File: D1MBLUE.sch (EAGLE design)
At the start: 7 parts, among them U1 HC_05

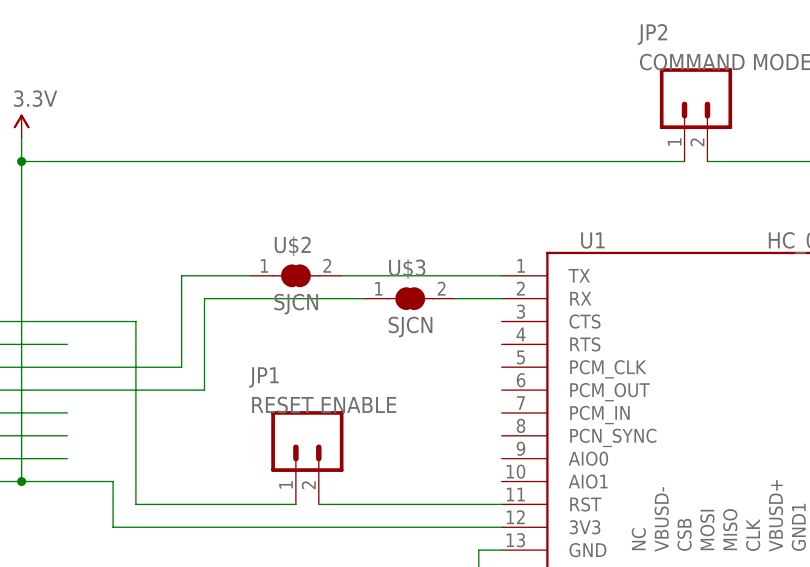
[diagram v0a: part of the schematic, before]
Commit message: Improved silkscreen and updated preview images
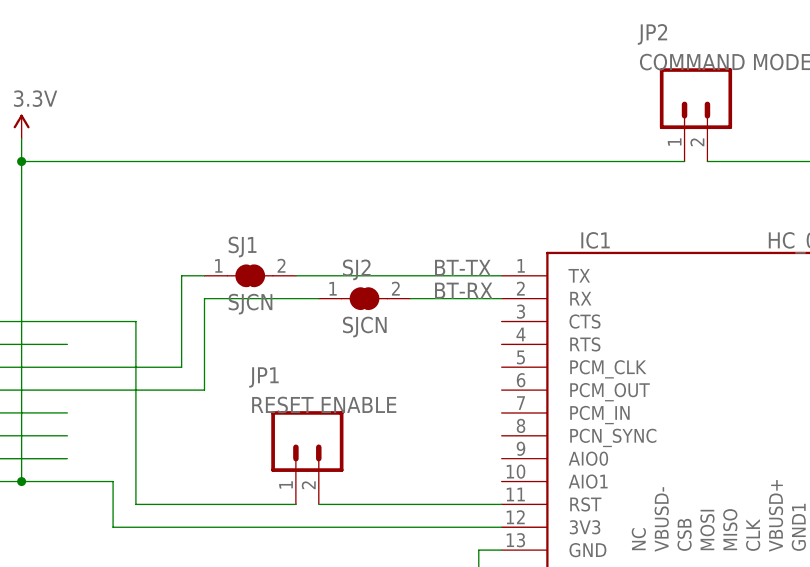
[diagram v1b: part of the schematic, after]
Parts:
- removed U$2, U$3: SJCN, freetronics-jon:SJCN
- added SJ1, SJ2: SJCN, freetronics-jon:SJCN
- renumbered U1 to IC1
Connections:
- removed net N$2: IC1.TX, U$2.2
- removed net N$4: IC1.RX, U$3.2
- new net BT-RX: IC1.RX, SJ2.2
- new net BT-TX: IC1.TX, SJ1.2
- net D0: now also SJ1.1; no longer U$2.1
- net D5: now also SJ2.1; no longer U$3.1
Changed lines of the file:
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@@
 <part name="P+1" library="freetronics-original" deviceset="3.3V" device=""/>
 <part name="GND1" library="freetronics-original" deviceset="GND" device=""/>
-<part name="U1" library="freetronics-jon" deviceset="HC_05" device=""/>
+<part name="IC1" library="freetronics-jon" deviceset="HC_05" device=""/>
 <part name="GND2" library="freetronics-original" deviceset="GND" device=""/>
 <part name="JP1" library="freetronics-jon" deviceset="M02" device="PTH" value="RESET ENABLE"/>
 <part name="JP2" library="freetronics-jon" deviceset="M02" device="PTH" value="COMMAND MODE"/>
-<part name="U$2" library="freetronics-jon" deviceset="SJC" device="N"/>
-<part name="U$3" library="freetronics-jon" deviceset="SJC" device="N"/>
+<part name="SJ1" library="freetronics-jon" deviceset="SJC" device="N"/>
+<part name="SJ2" library="freetronics-jon" deviceset="SJC" device="N"/>
 </parts>
 <sheets>
@@
 <instance part="P+1" gate="G$1" x="45.72" y="132.08"/>
 <instance part="GND1" gate="1" x="208.28" y="83.82"/>
-<instance part="U1" gate="G$1" x="121.92" y="101.6"/>
+<instance part="IC1" gate="G$1" x="121.92" y="101.6"/>
 <instance part="GND2" gate="1" x="149.86" y="71.12"/>
 <instance part="JP1" gate="G$1" x="76.2" y="99.06" smashed="yes" rot="R270">
@@
 <attribute name="NAME" x="114.3" y="143.002" size="1.778" layer="95"/>
 </instance>
-<instance part="U$2" gate="G$1" x="76.2" y="116.84"/>
-<instance part="U$3" gate="G$1" x="88.9" y="114.3"/>
+<instance part="SJ1" gate="G$1" x="71.12" y="116.84"/>
+<instance part="SJ2" gate="G$1" x="83.82" y="114.3"/>
 </instances>
 <busses>
@@
 </segment>
 <segment>
-<pinref part="U1" gate="G$1" pin="GND2"/>
+<pinref part="IC1" gate="G$1" pin="GND2"/>
 <pinref part="GND2" gate="1" pin="GND"/>
 <wire x1="147.32" y1="86.36" x2="149.86" y2="86.36" width="0.1524" layer="91"/>
 <wire x1="149.86" y1="86.36" x2="149.86" y2="76.2" width="0.1524" layer="91"/>
-<pinref part="U1" gate="G$1" pin="GND1"/>
+<pinref part="IC1" gate="G$1" pin="GND1"/>
 <wire x1="149.86" y1="76.2" x2="149.86" y2="73.66" width="0.1524" layer="91"/>
 <wire x1="132.08" y1="78.74" x2="132.08" y2="76.2" width="0.1524" layer="91"/>
 <wire x1="132.08" y1="76.2" x2="149.86" y2="76.2" width="0.1524" layer="91"/>
-<pinref part="U1" gate="G$1" pin="GND"/>
+<pinref part="IC1" gate="G$1" pin="GND"/>
 <wire x1="99.06" y1="86.36" x2="96.52" y2="86.36" width="0.1524" layer="91"/>
 <wire x1="96.52" y1="86.36" x2="96.52" y2="76.2" width="0.1524" layer="91"/>
@@
 <wire x1="31.75" y1="104.14" x2="66.04" y2="104.14" width="0.1524" layer="91"/>
 <label x="33.02" y="104.14" size="1.778" layer="95"/>
-<pinref part="U$3" gate="G$1" pin="1"/>
-<wire x1="83.82" y1="114.3" x2="66.04" y2="114.3" width="0.1524" layer="91"/>
+<pinref part="SJ2" gate="G$1" pin="1"/>
+<wire x1="78.74" y1="114.3" x2="66.04" y2="114.3" width="0.1524" layer="91"/>
 <wire x1="66.04" y1="114.3" x2="66.04" y2="104.14" width="0.1524" layer="91"/>
 </segment>
@@
 <label x="33.02" y="106.68" size="1.778" layer="95"/>
 <wire x1="63.5" y1="106.68" x2="63.5" y2="116.84" width="0.1524" layer="91"/>
-<pinref part="U$2" gate="G$1" pin="1"/>
-<wire x1="63.5" y1="116.84" x2="71.12" y2="116.84" width="0.1524" layer="91"/>
+<pinref part="SJ1" gate="G$1" pin="1"/>
+<wire x1="63.5" y1="116.84" x2="66.04" y2="116.84" width="0.1524" layer="91"/>
 </segment>
 </net>
@@
 <wire x1="45.72" y1="93.98" x2="45.72" y2="129.54" width="0.1524" layer="91"/>
 <junction x="45.72" y="93.98"/>
-<pinref part="U1" gate="G$1" pin="3V3"/>
+<pinref part="IC1" gate="G$1" pin="3V3"/>
 <wire x1="45.72" y1="129.54" x2="45.72" y2="132.08" width="0.1524" layer="91"/>
 <wire x1="99.06" y1="88.9" x2="55.88" y2="88.9" width="0.1524" layer="91"/>
@@
 <net name="N$1" class="0">
 <segment>
-<pinref part="U1" gate="G$1" pin="RST"/>
+<pinref part="IC1" gate="G$1" pin="RST"/>
 <wire x1="99.06" y1="91.44" x2="78.74" y2="91.44" width="0.1524" layer="91"/>
 <pinref part="JP1" gate="G$1" pin="2"/>
@@
 <net name="N$3" class="0">
 <segment>
-<pinref part="U1" gate="G$1" pin="PIO11"/>
+<pinref part="IC1" gate="G$1" pin="PIO11"/>
 <wire x1="147.32" y1="116.84" x2="149.86" y2="116.84" width="0.1524" layer="91"/>
 <wire x1="149.86" y1="116.84" x2="149.86" y2="129.54" width="0.1524" layer="91"/>
@@
 </segment>
 </net>
-<net name="N$2" class="0">
-<segment>
-<pinref part="U1" gate="G$1" pin="TX"/>
-<wire x1="99.06" y1="116.84" x2="81.28" y2="116.84" width="0.1524" layer="91"/>
-<pinref part="U$2" gate="G$1" pin="2"/>
-</segment>
-</net>
-<net name="N$4" class="0">
-<segment>
-<pinref part="U1" gate="G$1" pin="RX"/>
-<pinref part="U$3" gate="G$1" pin="2"/>
-<wire x1="93.98" y1="114.3" x2="99.06" y2="114.3" width="0.1524" layer="91"/>
-</segment>
-</net>
+<net name="BT-TX" class="0">
+<segment>
+<pinref part="IC1" gate="G$1" pin="TX"/>
+<wire x1="99.06" y1="116.84" x2="76.2" y2="116.84" width="0.1524" layer="91"/>
+<pinref part="SJ1" gate="G$1" pin="2"/>
+<label x="91.44" y="116.84" size="1.778" layer="95"/>
+</segment>
+</net>
+<net name="BT-RX" class="0">
+<segment>
+<pinref part="IC1" gate="G$1" pin="RX"/>
+<pinref part="SJ2" gate="G$1" pin="2"/>
+<wire x1="88.9" y1="114.3" x2="99.06" y2="114.3" width="0.1524" layer="91"/>
+<label x="91.44" y="114.3" size="1.778" layer="95"/>
+</segment>
+</net>
